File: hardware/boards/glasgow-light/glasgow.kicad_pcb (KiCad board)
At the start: 2 copper layers, 190 parts, among them J1 USB_C_USB2.0, J10 AUX, J2 IDC-Header_2x5_P2.54mm, J3 IDC-Header_2x5_P2.54mm, J4 Conn_01x02, U1 LM358_DFN, U10 SN74LVC1T45DCKR, U11 SN74LVC1T45DCKR, U12 INA180A2, U15 TPD3S014, U16 SN74LVC1T45DCKR, U17 SN74LVC1T45DCKR, U18 SN74LVC1T45DCKR, U19 PCA6408APW, U31 TPS73101DBV, U36 TLV73312PQDRVR, U4 SN74LVC1T45DCKR, U5 ICE40UP5K-SG48ITR, U6 SN74LVC1T45DCKR, U7 GD32VF103, U8 TLV75533PDRVR, U9 SN74LVC1T45DCKR, Y1 8M

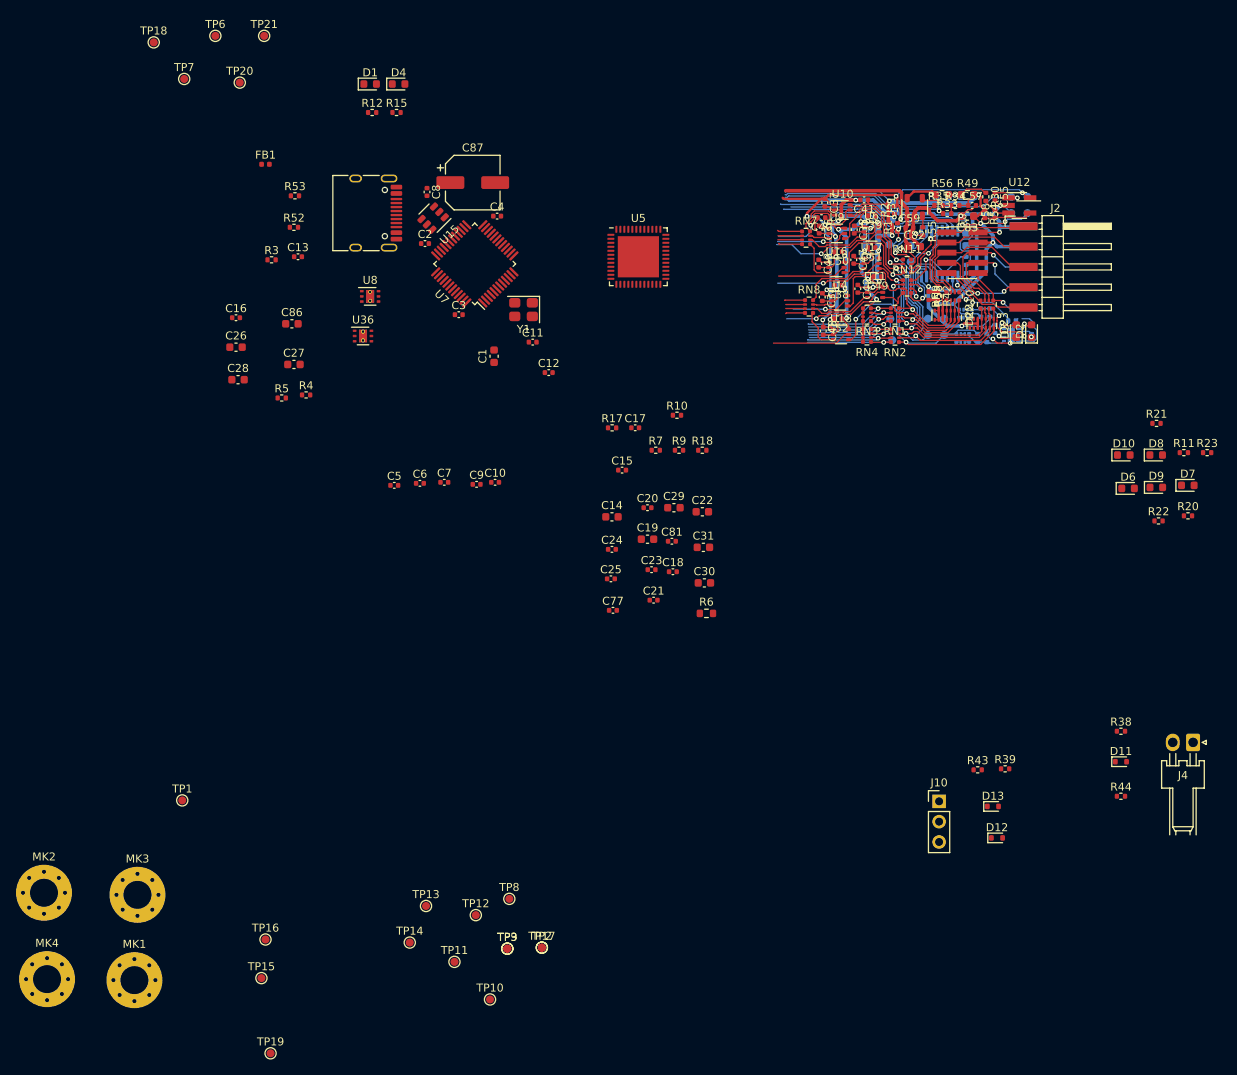
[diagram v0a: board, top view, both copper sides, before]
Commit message: start routing FPGA
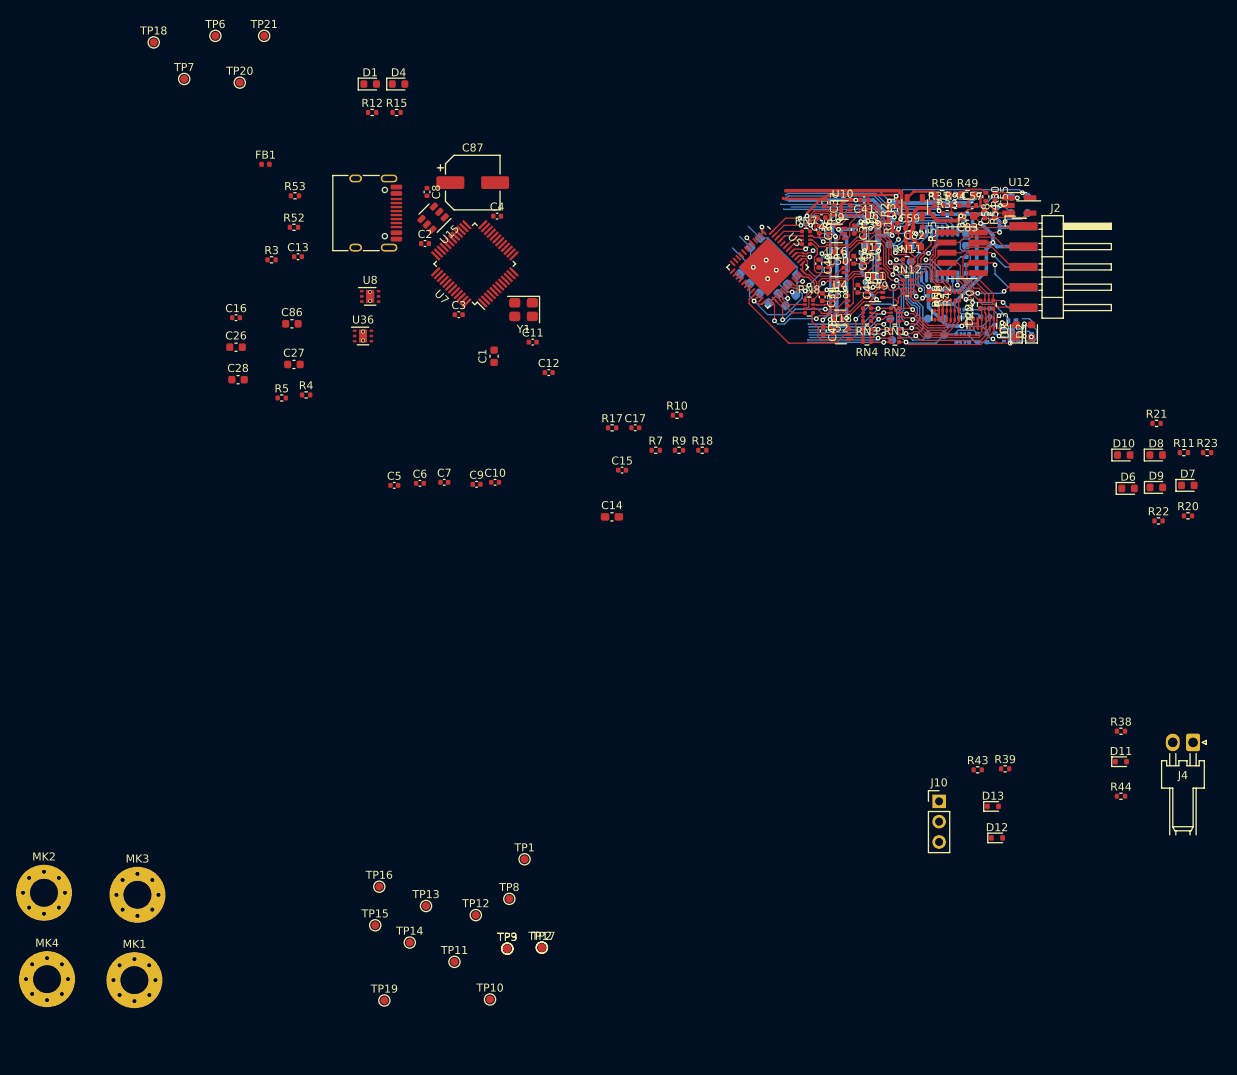
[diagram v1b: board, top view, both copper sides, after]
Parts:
- removed C18, C24, C25, C77, C81: u1, Capacitor_SMD:C_0402_1005Metric
- C14: footprint Capacitor_SMD:C_0603_1608Metric -> Capacitor_SMD:C_0603_1608Metric_Pad1.08x0.95mm_HandSolder
- C19, C22, C29, C30, C31: footprint Capacitor_SMD:C_0603_1608Metric -> Capacitor_SMD:C_0603_1608Metric_Pad1.08x0.95mm_HandSolder; moved to B.Cu
- C20, C21, C23: footprint Capacitor_SMD:C_0402_1005Metric -> Capacitor_SMD:C_0603_1608Metric_Pad1.08x0.95mm_HandSolder; moved to B.Cu
- R6: footprint Resistor_SMD:R_0603_1608Metric -> Resistor_SMD:R_0603_1608Metric_Pad0.98x0.95mm_HandSolder; moved to B.Cu
- moved C21 46.8 mm to (139.6, 41.1), turned to 315 degrees
- moved TP1 43.4 mm to (109.6, 118.1)
- moved C23 41.4 mm to (143.0, 44.5), turned to 135 degrees
- moved R6 40.5 mm to (142.9, 48.3), turned to 45 degrees
- moved C30 37.8 mm to (140.7, 46.8), turned to 135 degrees
- moved C19 36.3 mm to (138.3, 44.4), turned to 135 degrees
- moved C29 33.5 mm to (138.5, 42.2), turned to 315 degrees
- moved C31 32.1 mm to (139.5, 48.0), turned to 135 degrees
- moved C20 31.1 mm to (137.1, 45.5), turned to 135 degrees
- moved C22 30.7 mm to (141.9, 45.6), turned to 135 degrees
- moved U5 16.2 mm to (140.0, 44.1), turned to 315 degrees
- moved TP15 15.7 mm to (90.9, 126.4)
- moved TP16 15.7 mm to (91.4, 121.5)
- moved TP19 15.7 mm to (92.1, 135.8)
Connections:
- net /A0 renamed Net-(U5-Pad4)
- net /A1 renamed Net-(U5-Pad3)
- net /D6 renamed Net-(U5-Pad13)
- net /D7 renamed Net-(U5-Pad12)
- net /FLAGA renamed Net-(U5-Pad11)
- net /FLAGB renamed /~SYNC
- net /FLAGC renamed Net-(U5-Pad9)
- net /IO_Banks/QB6 renamed Net-(U5-Pad23)
- net /OE renamed Net-(U5-Pad6)
- net /PKTEND renamed Net-(U5-Pad2)
- RN7 pad 1: /IO_Banks/QA0 -> /QA6
- RN7 pad 2: /IO_Banks/QA1 -> /QA4
- RN7 pad 3: /IO_Banks/QA2 -> /QA2
- RN7 pad 4: /IO_Banks/QA3 -> /QA3
- RN8 pad 1: /IO_Banks/QA4 -> /QA4
- RN8 pad 2: /IO_Banks/QA5 -> /QA0
- RN8 pad 3: /IO_Banks/QA6 -> /QA1
- RN8 pad 4: /IO_Banks/QA7 -> /QA7
- U10 pad 5: /IO_Banks/DA6 -> /DA6
- U11 pad 5: /IO_Banks/DA1 -> /DA1
- U16 pad 5: /IO_Banks/DA3 -> /DA3
- U17 pad 5: /IO_Banks/DA5 -> /DA5
- U18 pad 5: /IO_Banks/DA7 -> /DA7
- U4 pad 5: /IO_Banks/DA0 -> /DA0
- U5 pad 14: /D5 -> FPGA_MISO
- U5 pad 15: /D4 -> FPGA_SCK
- U5 pad 16: /D3 -> FPGA_CS
- U5 pad 17: /D2 -> FPGA_MOSI
- U5 pad 18: /D1 -> /SDA
- U5 pad 19: /D0 -> /SCL
- U5 pad 20: /CLKIF -> FPGA_SCK
- U5 pad 21: /QB7 -> /DA7
- U5 pad 25: /IO_Banks/QB5 -> /DA1
- U5 pad 26: /IO_Banks/QB4 -> /DA0
- U5 pad 27: /IO_Banks/QB3 -> /QA7
- U5 pad 28: /IO_Banks/QB2 -> /QA0
- U5 pad 31: /IO_Banks/QB1 -> /DA5
- U5 pad 32: /IO_Banks/QB0 -> /DA2
- U5 pad 34: /IO_Banks/QA7 -> /QA4
- U5 pad 35: /IO_Banks/QA6 -> /QA4
- U5 pad 36: /IO_Banks/QA5 -> /QA6
- U5 pad 37: /IO_Banks/QA4 -> /QA6
- U5 pad 38: /IO_Banks/QA3 -> /DA3
- U5 pad 39: /SCL -> Net-(U5-Pad39)
- U5 pad 40: /SDA -> Net-(U5-Pad40)
- U5 pad 41: /IO_Banks/~SYNC -> Net-(U5-Pad41)
- U5 pad 42: /IO_Banks/QA2 -> /QA3
- U5 pad 43: /IO_Banks/QA1 -> /QA2
- U5 pad 45: /QA0 -> /QA1
- U5 pad 46: /WR -> /QA0
- U5 pad 47: /RD -> /DA6
- U5 pad 48: /FLAGD -> /DA4
- U6 pad 5: /IO_Banks/DA2 -> /DA2
- U9 pad 5: /IO_Banks/DA4 -> /DA4
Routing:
- net +3V3: track 127.9 -> 158.4 mm, vias 13 -> 16
- net GND: track 211.7 -> 232.7 mm, vias 17 -> 21
- net /DA1: track 0.00 -> 17.9 mm, vias 0 -> 2
- net /DA7: track 0.00 -> 16.5 mm
- net /DA2: track 0.00 -> 15.3 mm, vias 0 -> 2
- net /IO_Banks/DA2: track 14.4 -> 0.00 mm, vias 1 -> 0
- net +1V2: track 0.00 -> 14.3 mm, vias 0 -> 2
- net /IO_Banks/DA5: track 13.6 -> 0.00 mm, vias 1 -> 0
- net /IO_Banks/DA1: track 13.5 -> 0.00 mm, vias 1 -> 0
- net /IO_Banks/DA6: track 13.4 -> 0.00 mm, vias 1 -> 0
- net /DA6: track 0.00 -> 13.4 mm, vias 0 -> 2
- net /DA5: track 0.00 -> 12.9 mm, vias 0 -> 2
- net /DA4: track 0.00 -> 12.7 mm, vias 0 -> 2
- net /DA0: track 0.00 -> 12.2 mm, vias 0 -> 2
- net /IO_Banks/DA7: track 9.84 -> 0.00 mm
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
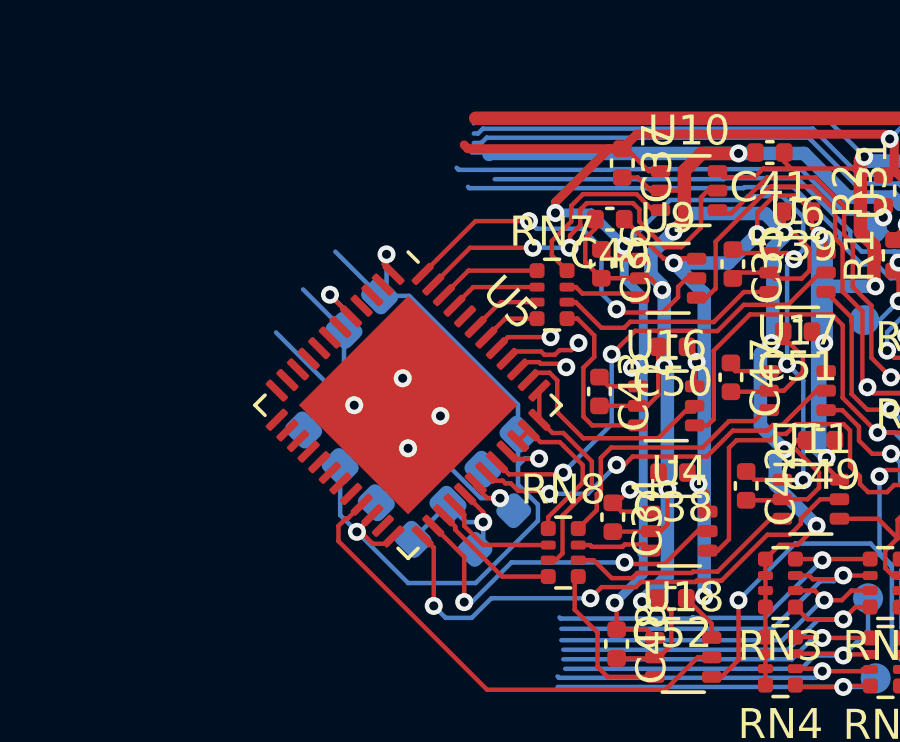
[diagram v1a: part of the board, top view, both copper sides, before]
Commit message: right side of FPGA routed
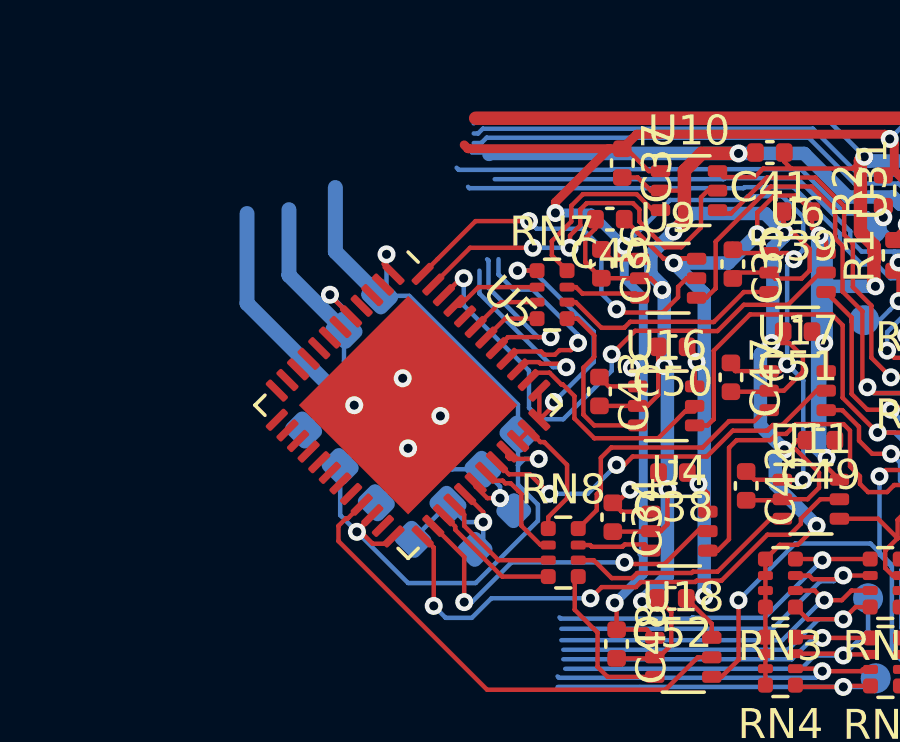
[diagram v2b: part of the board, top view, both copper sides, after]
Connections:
- RN8 pad 1: /QA4 -> /QA5
- U5 pad 28: /QA0 -> /QA1
- U5 pad 31: /DA5 -> /QA0
- U5 pad 32: /DA2 -> /DA5
- U5 pad 34: /QA4 -> /QA5
- U5 pad 35: /QA4 -> /QA5
- U5 pad 45: /QA1 -> /QA4
- U5 pad 46: /QA0 -> /DA2
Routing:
- net Net-(U5-Pad39): track 1.78 -> 6.45 mm
- net /QA5: track 0.00 -> 4.64 mm
- net GND: track 232.7 -> 237.1 mm
- net Net-(U5-Pad40): track 2.67 -> 6.92 mm
- net Net-(U5-Pad41): track 1.94 -> 5.67 mm
- net /QA0: track 7.35 -> 3.68 mm
- net /DA2: track 15.3 -> 18.5 mm
- net +1V2: track 14.3 -> 17.3 mm
- net /QA4: track 5.37 -> 3.01 mm
- net +3V3: track 158.4 -> 160.6 mm
- net /QA6: track 7.33 -> 8.70 mm, vias 0 -> 2
- net /QA1: track 3.01 -> 4.12 mm

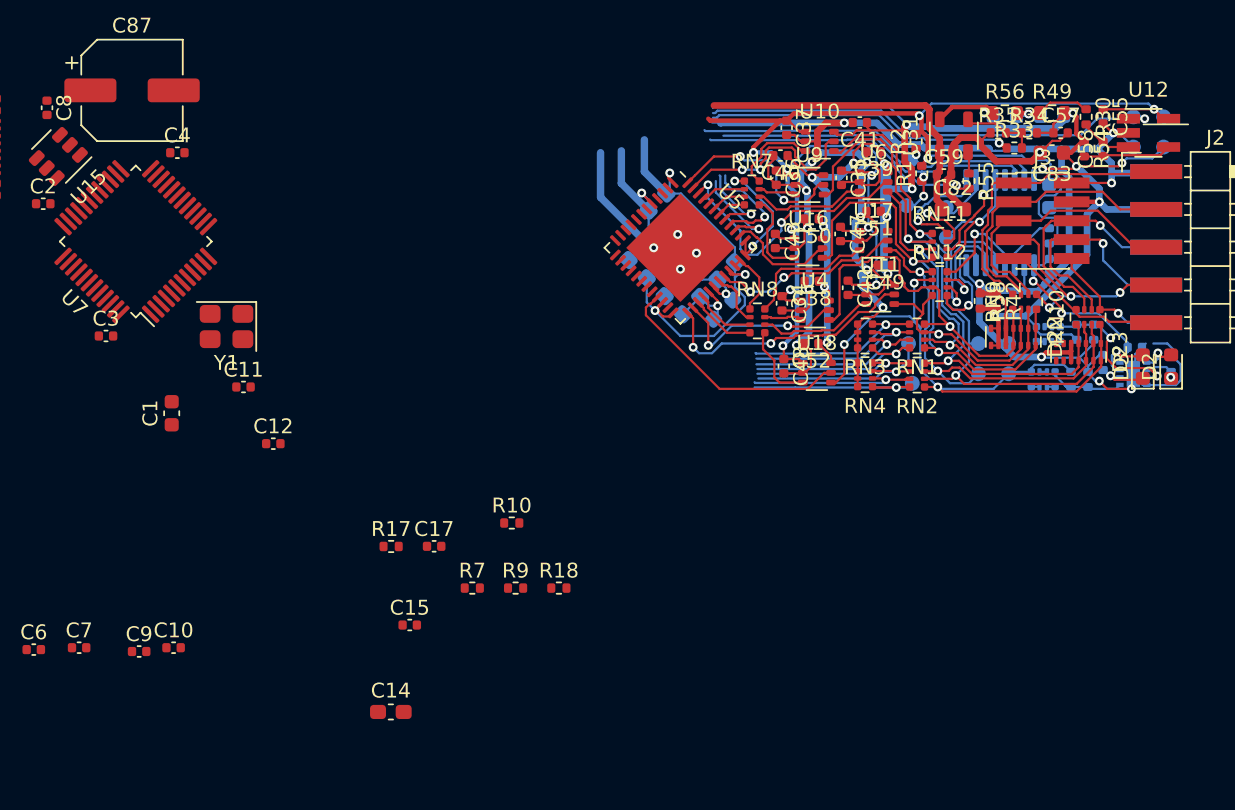
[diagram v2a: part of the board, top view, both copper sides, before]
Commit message: continue routing around FPGA
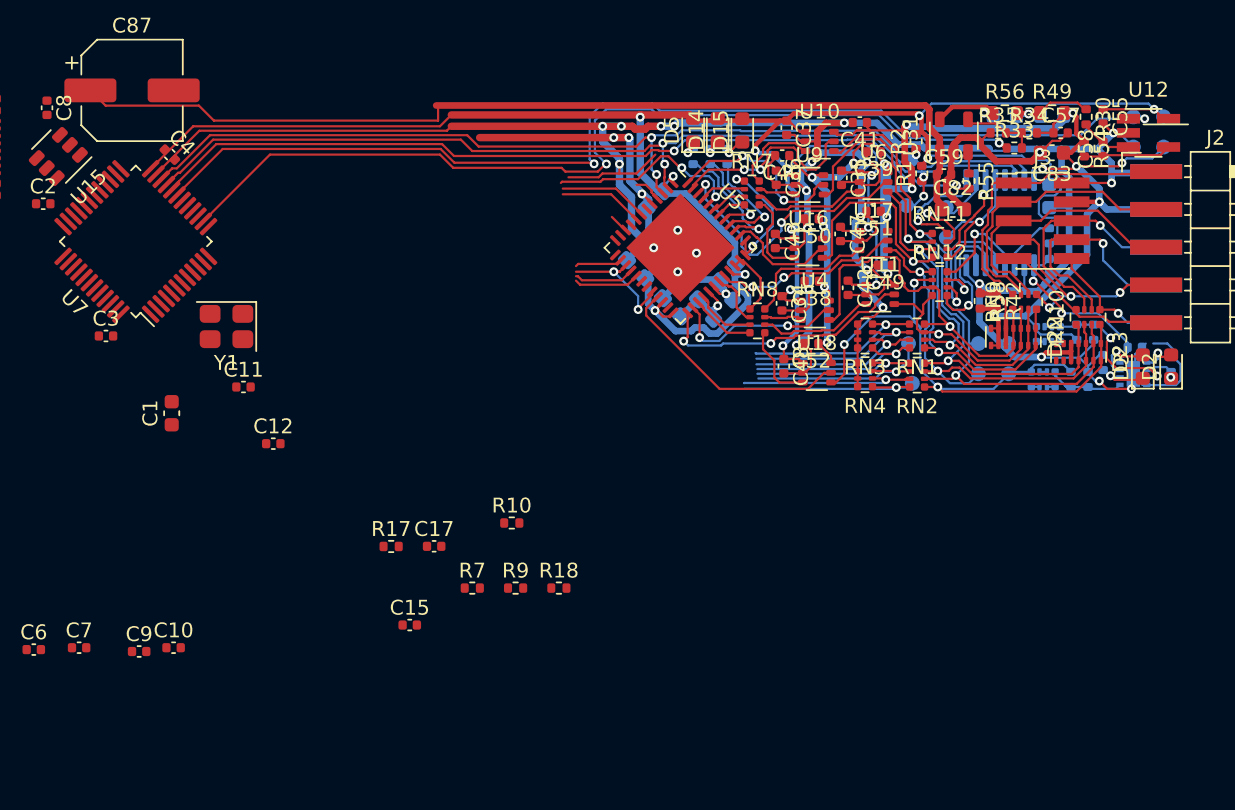
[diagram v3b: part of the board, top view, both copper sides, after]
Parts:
- added D14: YEL, LED_SMD:LED_0603_1608Metric, F.Cu at (142.5, 36.2)
- added D15: YEL, LED_SMD:LED_0603_1608Metric, F.Cu at (144.1, 36.2)
- added D5: YEL, LED_SMD:LED_0603_1608Metric, F.Cu at (140.8, 36.2)
- added R26: 0, Resistor_SMD:R_0402_1005Metric, B.Cu at (140.8, 38.0)
- added R27: 0, Resistor_SMD:R_0402_1005Metric, B.Cu at (142.0, 38.0)
- added R28: 0, Resistor_SMD:R_0402_1005Metric, B.Cu at (143.1, 38.0)
- C14: moved to B.Cu
- moved C14 37.8 mm to (140.7, 43.3), turned to 45 degrees
- moved C4 0.52 mm to (105.7, 37.8), turned to 315 degrees
- moved C21 0.24 mm to (139.5, 40.9)
- moved C30 0.22 mm to (140.6, 47.0)
- moved C29 0.21 mm to (138.3, 42.1)
- moved C31 0.18 mm to (139.4, 48.1)
- moved C22 0.17 mm to (142.0, 45.7)
- moved C19 0.13 mm to (138.2, 44.4)
- moved C40 0.12 mm to (146.8, 37.9)
- moved C20 0.11 mm to (137.0, 45.5)
- moved C23 0.10 mm to (143.1, 44.6)
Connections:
- U5 pad 18: /SDA -> Net-(U5-Pad18)
- U5 pad 19: /SCL -> Net-(U5-Pad19)
- U5 pad 2: Net-(U5-Pad2) -> /SCL
- U5 pad 3: Net-(U5-Pad3) -> /SDA
- U5 pad 39: Net-(U5-Pad39) -> /LED0
- U5 pad 40: Net-(U5-Pad40) -> /LED2
- U5 pad 41: Net-(U5-Pad41) -> /LED1
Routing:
- net GND: track 237.1 -> 283.2 mm, vias 21 -> 26
- net +3V3: track 160.6 -> 205.7 mm, vias 16 -> 17
- net +5V: track 21.8 -> 65.8 mm
- net /SDA: track 24.3 -> 66.9 mm, vias 1 -> 3
- net /SCL: track 24.3 -> 67.0 mm, vias 2 -> 4
- net VIO_CURRENT: track 32.3 -> 74.1 mm, vias 1 -> 2
- net VIO_DAC: track 20.7 -> 62.0 mm, vias 1 -> 2
- net VIO_ENA: track 19.0 -> 57.3 mm, vias 1 -> 2
- net /IO_Banks/VIOA: track 157.5 -> 143.0 mm
- net /CLKREF: track 0.00 -> 13.5 mm, vias 0 -> 2
- net +1V2: track 17.3 -> 29.4 mm, vias 2 -> 4
- net FPGA_SCK: track 0.00 -> 8.72 mm, vias 0 -> 2
- net /LED0: track 0.00 -> 8.41 mm, vias 0 -> 1
- net /LED2: track 0.00 -> 7.37 mm, vias 0 -> 1
- net Net-(U5-Pad40): track 6.92 -> 0.00 mm, vias 1 -> 0
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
